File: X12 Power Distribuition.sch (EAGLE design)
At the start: 47 parts, among them Q1 SPB80P06P, Y1 ECS-80-S-4X

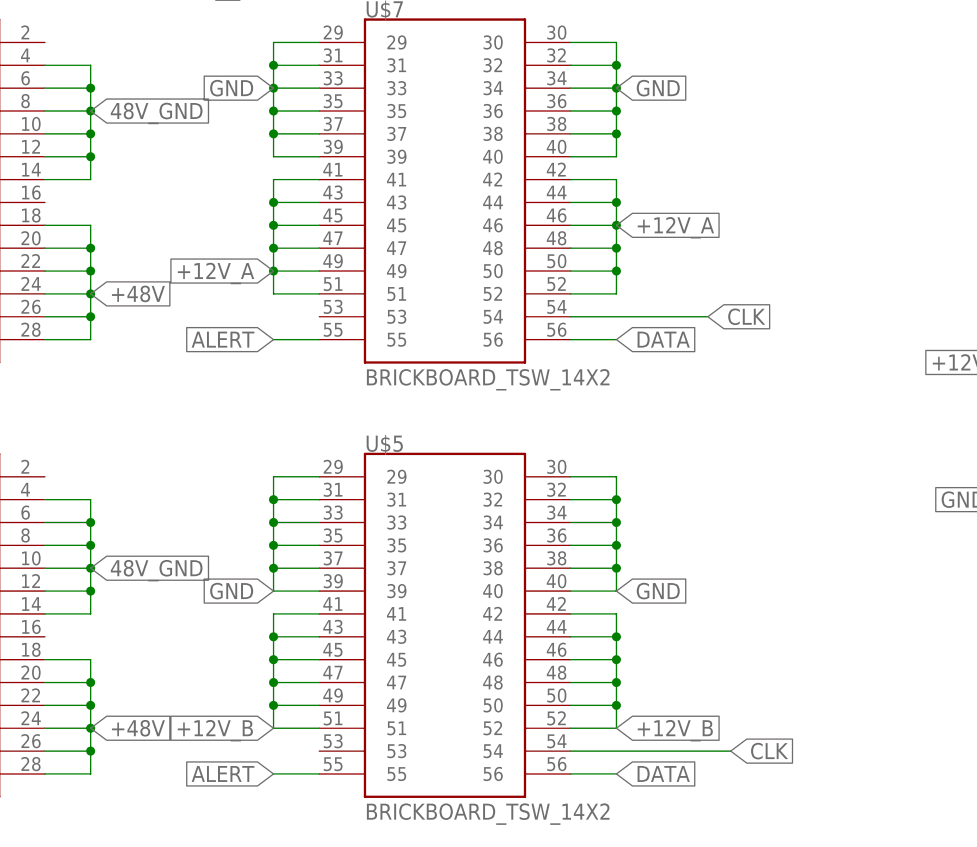
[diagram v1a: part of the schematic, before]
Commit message: Changed Brick Connectors
Moved the data signals on brick to middle of connector
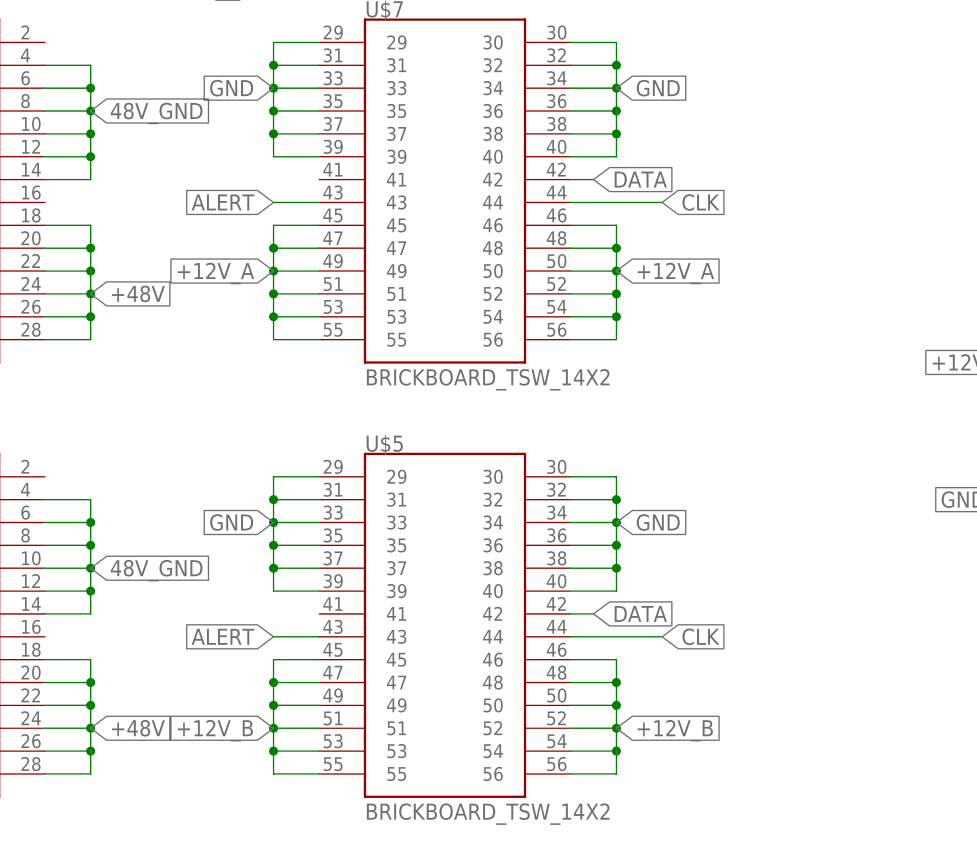
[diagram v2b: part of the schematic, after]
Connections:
- net +12V_A: now also U$7.53, U$7.54, U$7.55, U$7.56; no longer U$7.41, U$7.42, U$7.43, U$7.44
- net +12V_B: now also U$5.53, U$5.54, U$5.55, U$5.56; no longer U$5.41, U$5.42, U$5.43, U$5.44
- net ALERT: now also U$5.43, U$7.43; no longer U$5.55, U$7.55
- net CLK: now also U$5.44, U$7.44; no longer U$5.54, U$7.54
- net DATA: now also U$5.42, U$7.42; no longer U$5.56, U$7.56
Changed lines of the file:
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@@
 <pinref part="U$7" gate="G$1" pin="50"/>
 <pinref part="U$7" gate="G$1" pin="52"/>
-<pinref part="U$7" gate="G$1" pin="44"/>
-<wire x1="132.08" y1="73.66" x2="137.16" y2="73.66" width="0.1524" layer="91"/>
-<wire x1="137.16" y1="73.66" x2="137.16" y2="71.12" width="0.1524" layer="91"/>
-<junction x="137.16" y="71.12"/>
-<pinref part="U$7" gate="G$1" pin="42"/>
-<wire x1="132.08" y1="76.2" x2="137.16" y2="76.2" width="0.1524" layer="91"/>
-<wire x1="137.16" y1="76.2" x2="137.16" y2="73.66" width="0.1524" layer="91"/>
-<junction x="137.16" y="73.66"/>
-<label x="137.16" y="71.12" size="1.778" layer="95" xref="yes"/>
+<label x="137.16" y="66.04" size="1.778" layer="95" xref="yes"/>
+<pinref part="U$7" gate="G$1" pin="56"/>
+<wire x1="132.08" y1="58.42" x2="137.16" y2="58.42" width="0.1524" layer="91"/>
+<wire x1="137.16" y1="58.42" x2="137.16" y2="60.96" width="0.1524" layer="91"/>
+<junction x="137.16" y="63.5"/>
+<pinref part="U$7" gate="G$1" pin="54"/>
+<wire x1="137.16" y1="60.96" x2="137.16" y2="63.5" width="0.1524" layer="91"/>
+<wire x1="132.08" y1="60.96" x2="137.16" y2="60.96" width="0.1524" layer="91"/>
+<junction x="137.16" y="60.96"/>
 </segment>
 <segment>
@@
 <pinref part="U$7" gate="G$1" pin="51"/>
 <label x="99.06" y="66.04" size="1.778" layer="95" rot="R180" xref="yes"/>
-<pinref part="U$7" gate="G$1" pin="41"/>
-<wire x1="104.14" y1="76.2" x2="99.06" y2="76.2" width="0.1524" layer="91"/>
-<wire x1="99.06" y1="76.2" x2="99.06" y2="73.66" width="0.1524" layer="91"/>
-<pinref part="U$7" gate="G$1" pin="43"/>
-<wire x1="99.06" y1="73.66" x2="104.14" y2="73.66" width="0.1524" layer="91"/>
-<wire x1="99.06" y1="73.66" x2="99.06" y2="71.12" width="0.1524" layer="91"/>
-<junction x="99.06" y="73.66"/>
-<junction x="99.06" y="71.12"/>
+<pinref part="U$7" gate="G$1" pin="53"/>
+<wire x1="104.14" y1="60.96" x2="99.06" y2="60.96" width="0.1524" layer="91"/>
+<wire x1="99.06" y1="60.96" x2="99.06" y2="63.5" width="0.1524" layer="91"/>
+<junction x="99.06" y="63.5"/>
+<pinref part="U$7" gate="G$1" pin="55"/>
+<wire x1="104.14" y1="58.42" x2="99.06" y2="58.42" width="0.1524" layer="91"/>
+<wire x1="99.06" y1="58.42" x2="99.06" y2="60.96" width="0.1524" layer="91"/>
+<junction x="99.06" y="60.96"/>
 </segment>
 </net>
@@
 <pinref part="U$5" gate="G$1" pin="52"/>
 <label x="137.16" y="15.24" size="1.778" layer="95" xref="yes"/>
-<pinref part="U$5" gate="G$1" pin="44"/>
-<wire x1="132.08" y1="25.4" x2="137.16" y2="25.4" width="0.1524" layer="91"/>
-<wire x1="137.16" y1="25.4" x2="137.16" y2="22.86" width="0.1524" layer="91"/>
-<junction x="137.16" y="22.86"/>
-<wire x1="137.16" y1="25.4" x2="137.16" y2="27.94" width="0.1524" layer="91"/>
-<junction x="137.16" y="25.4"/>
-<pinref part="U$5" gate="G$1" pin="42"/>
-<wire x1="137.16" y1="27.94" x2="132.08" y2="27.94" width="0.1524" layer="91"/>
+<pinref part="U$5" gate="G$1" pin="54"/>
+<wire x1="132.08" y1="12.7" x2="137.16" y2="12.7" width="0.1524" layer="91"/>
+<wire x1="137.16" y1="12.7" x2="137.16" y2="15.24" width="0.1524" layer="91"/>
+<junction x="137.16" y="15.24"/>
+<pinref part="U$5" gate="G$1" pin="56"/>
+<wire x1="132.08" y1="10.16" x2="137.16" y2="10.16" width="0.1524" layer="91"/>
+<wire x1="137.16" y1="10.16" x2="137.16" y2="12.7" width="0.1524" layer="91"/>
+<junction x="137.16" y="12.7"/>
 </segment>
 <segment>
@@
 <pinref part="U$5" gate="G$1" pin="51"/>
 <label x="99.06" y="15.24" size="1.778" layer="95" rot="R180" xref="yes"/>
-<pinref part="U$5" gate="G$1" pin="43"/>
-<wire x1="104.14" y1="25.4" x2="99.06" y2="25.4" width="0.1524" layer="91"/>
-<wire x1="99.06" y1="25.4" x2="99.06" y2="22.86" width="0.1524" layer="91"/>
-<junction x="99.06" y="22.86"/>
-<pinref part="U$5" gate="G$1" pin="41"/>
-<wire x1="104.14" y1="27.94" x2="99.06" y2="27.94" width="0.1524" layer="91"/>
-<wire x1="99.06" y1="27.94" x2="99.06" y2="25.4" width="0.1524" layer="91"/>
-<junction x="99.06" y="25.4"/>
+<pinref part="U$5" gate="G$1" pin="53"/>
+<wire x1="104.14" y1="12.7" x2="99.06" y2="12.7" width="0.1524" layer="91"/>
+<wire x1="99.06" y1="12.7" x2="99.06" y2="15.24" width="0.1524" layer="91"/>
+<junction x="99.06" y="15.24"/>
+<pinref part="U$5" gate="G$1" pin="55"/>
+<wire x1="104.14" y1="10.16" x2="99.06" y2="10.16" width="0.1524" layer="91"/>
+<wire x1="99.06" y1="10.16" x2="99.06" y2="12.7" width="0.1524" layer="91"/>
+<junction x="99.06" y="12.7"/>
 </segment>
 </net>
@@
 <pinref part="U$5" gate="G$1" pin="37"/>
 <pinref part="U$5" gate="G$1" pin="39"/>
-<label x="99.06" y="30.48" size="1.778" layer="95" rot="R180" xref="yes"/>
 <wire x1="99.06" y1="40.64" x2="99.06" y2="38.1" width="0.1524" layer="91"/>
 <junction x="99.06" y="38.1"/>
@@
 <wire x1="99.06" y1="40.64" x2="99.06" y2="43.18" width="0.1524" layer="91"/>
 <junction x="99.06" y="40.64"/>
+<label x="99.06" y="38.1" size="1.778" layer="95" rot="R180" xref="yes"/>
 </segment>
 <segment>
@@
 <pinref part="U$5" gate="G$1" pin="38"/>
 <pinref part="U$5" gate="G$1" pin="40"/>
-<label x="137.16" y="30.48" size="1.778" layer="95" xref="yes"/>
 <wire x1="137.16" y1="40.64" x2="137.16" y2="38.1" width="0.1524" layer="91"/>
 <junction x="137.16" y="38.1"/>
 <wire x1="137.16" y1="43.18" x2="137.16" y2="40.64" width="0.1524" layer="91"/>
 <junction x="137.16" y="40.64"/>
+<label x="137.16" y="38.1" size="1.778" layer="95" xref="yes"/>
 </segment>
 </net>
@@
 </segment>
 <segment>
-<pinref part="U$7" gate="G$1" pin="56"/>
-<wire x1="132.08" y1="58.42" x2="137.16" y2="58.42" width="0.1524" layer="91"/>
-<label x="137.16" y="58.42" size="1.778" layer="95" xref="yes"/>
-</segment>
-<segment>
-<pinref part="U$5" gate="G$1" pin="56"/>
-<wire x1="132.08" y1="10.16" x2="137.16" y2="10.16" width="0.1524" layer="91"/>
-<label x="137.16" y="10.16" size="1.778" layer="95" xref="yes"/>
+<pinref part="U$7" gate="G$1" pin="42"/>
+<wire x1="132.08" y1="76.2" x2="134.62" y2="76.2" width="0.1524" layer="91"/>
+<label x="134.62" y="76.2" size="1.778" layer="95" xref="yes"/>
+</segment>
+<segment>
+<pinref part="U$5" gate="G$1" pin="42"/>
+<wire x1="132.08" y1="27.94" x2="134.62" y2="27.94" width="0.1524" layer="91"/>
+<label x="134.62" y="27.94" size="1.778" layer="95" xref="yes"/>
 </segment>
 </net>
@@
 </segment>
 <segment>
-<pinref part="U$7" gate="G$1" pin="54"/>
-<wire x1="132.08" y1="60.96" x2="147.32" y2="60.96" width="0.1524" layer="91"/>
-<label x="147.32" y="60.96" size="1.778" layer="95" xref="yes"/>
-</segment>
-<segment>
-<pinref part="U$5" gate="G$1" pin="54"/>
-<wire x1="132.08" y1="12.7" x2="149.86" y2="12.7" width="0.1524" layer="91"/>
-<label x="149.86" y="12.7" size="1.778" layer="95" xref="yes"/>
+<pinref part="U$7" gate="G$1" pin="44"/>
+<wire x1="132.08" y1="73.66" x2="142.24" y2="73.66" width="0.1524" layer="91"/>
+<label x="142.24" y="73.66" size="1.778" layer="95" xref="yes"/>
+</segment>
+<segment>
+<pinref part="U$5" gate="G$1" pin="44"/>
+<wire x1="132.08" y1="25.4" x2="142.24" y2="25.4" width="0.1524" layer="91"/>
+<label x="142.24" y="25.4" size="1.778" layer="95" xref="yes"/>
 </segment>
 </net>
@@
 </segment>
 <segment>
-<pinref part="U$7" gate="G$1" pin="55"/>
-<wire x1="104.14" y1="58.42" x2="99.06" y2="58.42" width="0.1524" layer="91"/>
-<label x="99.06" y="58.42" size="1.778" layer="95" rot="R180" xref="yes"/>
-</segment>
-<segment>
-<pinref part="U$5" gate="G$1" pin="55"/>
-<wire x1="104.14" y1="10.16" x2="99.06" y2="10.16" width="0.1524" layer="91"/>
-<label x="99.06" y="10.16" size="1.778" layer="95" rot="R180" xref="yes"/>
-</segment>
-</net>
+<pinref part="U$7" gate="G$1" pin="43"/>
+<wire x1="104.14" y1="73.66" x2="99.06" y2="73.66" width="0.1524" layer="91"/>
+<label x="99.06" y="73.66" size="1.778" layer="95" rot="R180" xref="yes"/>
+</segment>
+<segment>
+<pinref part="U$5" gate="G$1" pin="43"/>
+<wire x1="104.14" y1="25.4" x2="99.06" y2="25.4" width="0.1524" layer="91"/>
+<label x="99.06" y="25.4" size="1.778" layer="95" rot="R180" xref="yes"/>
+</segment>
+</net>
